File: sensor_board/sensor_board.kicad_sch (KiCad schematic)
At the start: 51 parts, among them J1 zigbee connector, J2 SWD, J3 USB_B_Micro, J4 AM2320, J5 Lithium_battery_conn, J6 ACC, Q1 DMP3098LQ, U1 MCP6002-xMC, U2 MIC5365-3.3YC5, U3 STM32L051C8Tx, U4 MIC5365-3.3YC5, U5 SDC42

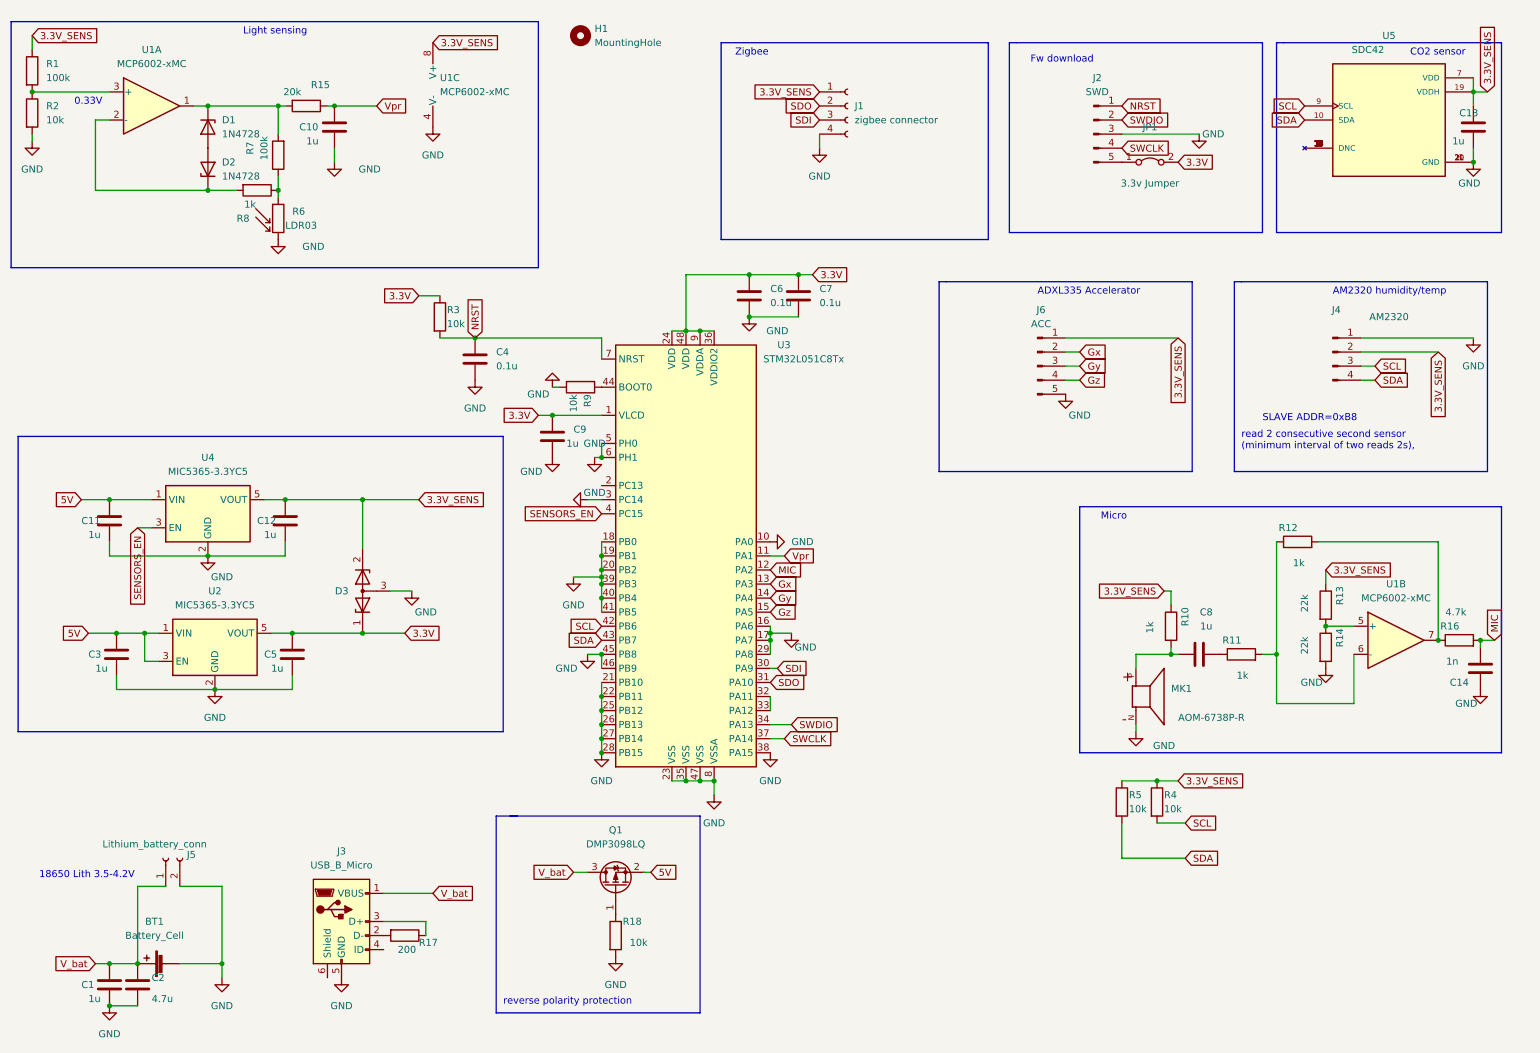
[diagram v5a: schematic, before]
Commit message: add testpoints
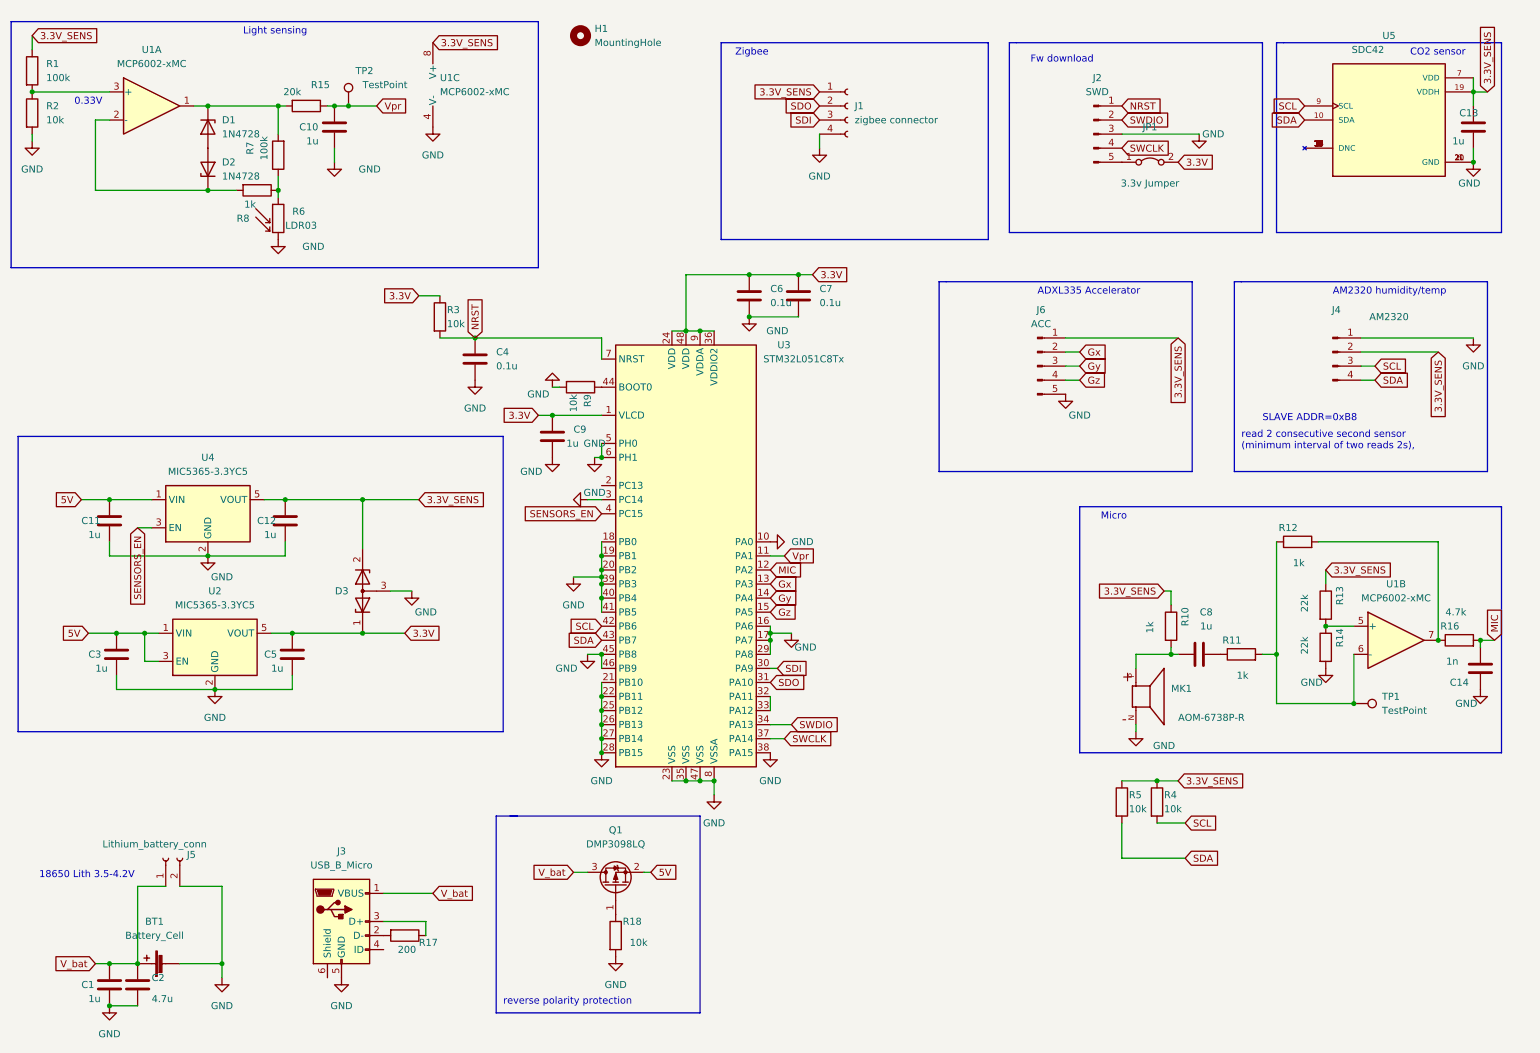
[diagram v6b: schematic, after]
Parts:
- added TP1, TP2: TestPoint, TestPoint:TestPoint_Loop_D2.60mm_Drill1.6mm_Beaded, symbol Connector:TestPoint
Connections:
- net Vpr: now also TP2.1
- net at R11.2, R12.1, U1.6 (-): now also TP1.1
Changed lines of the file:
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@@
   (junction (at 149.86 124.46) (diameter 0) (color 0 0 0 0)
   )
+  (junction (at 255.27 135.89) (diameter 0) (color 0 0 0 0)
+  )
   (junction (at 119.38 109.22) (diameter 0) (color 0 0 0 0)
   )
@@
   (junction (at 134.62 149.86) (diameter 0) (color 0 0 0 0)
   )
+  (junction (at 73.66 27.94) (diameter 0) (color 0 0 0 0)
+  )
   (junction (at 119.38 137.16) (diameter 0) (color 0 0 0 0)
   )
@@
     (stroke (width 0) (type default) (color 0 0 0 0))
   )
-  (wire (pts (xy 71.12 27.94) (xy 78.74 27.94))
+  (wire (pts (xy 71.12 27.94) (xy 73.66 27.94))
     (stroke (width 0) (type default) (color 0 0 0 0))
   )
@@
   )
   (wire (pts (xy 48.26 27.94) (xy 60.96 27.94))
+    (stroke (width 0) (type default) (color 0 0 0 0))
+  )
+  (wire (pts (xy 73.66 27.94) (xy 78.74 27.94))
     (stroke (width 0) (type default) (color 0 0 0 0))
   )
@@
     (pin "1")
   )
+  (symbol (lib_id "Connector:TestPoint") (at 255.27 135.89 270) (unit 1)
+    (in_bom yes) (on_board yes) (fields_autoplaced)
+    (property "Reference" "TP1" (id 0) (at 260.35 134.6199 90)
+      (effects (font (size 1.27 1.27)) (justify left))
+    )
+    (property "Value" "TestPoint" (id 1) (at 260.35 137.1599 90)
+      (effects (font (size 1.27 1.27)) (justify left))
+    )
+    (property "Footprint" "TestPoint:TestPoint_Loop_D2.60mm_Drill1.6mm_Beaded" (id 2) (at 255.27 140.97 0)
+      (effects (font (size 1.27 1.27)) hide)
+    )
+    (property "Datasheet" "~" (id 3) (at 255.27 140.97 0)
+      (effects (font (size 1.27 1.27)) hide)
+    )
+    (pin "1")
+  )
   (symbol (lib_id "Device:R") (at 219.71 153.67 0) (unit 1)
     (in_bom yes) (on_board yes)
@@
     (pin "N")
     (pin "P")
+  )
+  (symbol (lib_id "Connector:TestPoint") (at 73.66 27.94 0) (unit 1)
+    (in_bom yes) (on_board yes)
+    (property "Reference" "TP2" (id 0) (at 74.93 21.59 0)
+      (effects (font (size 1.27 1.27)) (justify left))
+    )
+    (property "Value" "TestPoint" (id 1) (at 76.2 24.13 0)
+      (effects (font (size 1.27 1.27)) (justify left))
+    )
+    (property "Footprint" "TestPoint:TestPoint_Loop_D2.60mm_Drill1.6mm_Beaded" (id 2) (at 78.74 27.94 0)
+      (effects (font (size 1.27 1.27)) hide)
+    )
+    (property "Datasheet" "~" (id 3) (at 78.74 27.94 0)
+      (effects (font (size 1.27 1.27)) hide)
+    )
+    (pin "1")
   )
   (symbol (lib_id "Amplifier_Operational:MCP6002-xMC") (at 38.1 27.94 0) (unit 1)
@@
       (reference "R18") (unit 1) (value "10k") (footprint "Resistor_SMD:R_0805_2012Metric_Pad1.20x1.40mm_HandSolder")
     )
+    (path "/6bf6eb53-f6b8-4bb3-bea3-e752d61d3186"
+      (reference "TP1") (unit 1) (value "TestPoint") (footprint "TestPoint:TestPoint_Loop_D2.60mm_Drill1.6mm_Beaded")
+    )
+    (path "/7bb33523-52b2-40e5-92e9-a8344a7aca40"
+      (reference "TP2") (unit 1) (value "TestPoint") (footprint "TestPoint:TestPoint_Loop_D2.60mm_Drill1.6mm_Beaded")
+    )
     (path "/7c1f2b6f-d99a-474b-9f6f-4bc67da4ff5c"

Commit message: add cap to ..
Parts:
- added C15, C16, C17: 0.1u, Capacitor_SMD:C_1206_3216Metric_Pad1.33x1.80mm_HandSolder, symbol Device:C
- added J7: DBG_PWR, TerminalBlock:TerminalBlock_bornier-2_P5.08mm, symbol Connector:Screw_Terminal_01x02
- added R19, R20: 470, Resistor_SMD:R_0805_2012Metric_Pad1.20x1.40mm_HandSolder, symbol Device:R
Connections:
- net 5V: now also J7.2 (Pin_2)
- net GND: now also C15.1, C16.1, C17.1, J7.1 (Pin_1)
- net Gx: now also C15.2
- net Gy: now also C16.2
- net Gz: now also C17.2
- net SWCLK: now also R19.2; no longer J2.4 (Pin_4)
- net SWDIO: now also R20.2; no longer J2.2 (Pin_2)
- new net: J2.2 (Pin_2), R20.1
- new net: J2.4 (Pin_4), R19.1
